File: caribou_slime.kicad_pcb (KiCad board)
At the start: 2 copper layers, 62.7 x 37.6 mm, 37 parts, among them J1 BATT JST, Q1 AO3145, U1 ESP32-C3_SUPERMINI, U2 BMI270, U3 FS312F-G, U4 FS8205A, U5 TP4056, U6 ME6211C33M5G

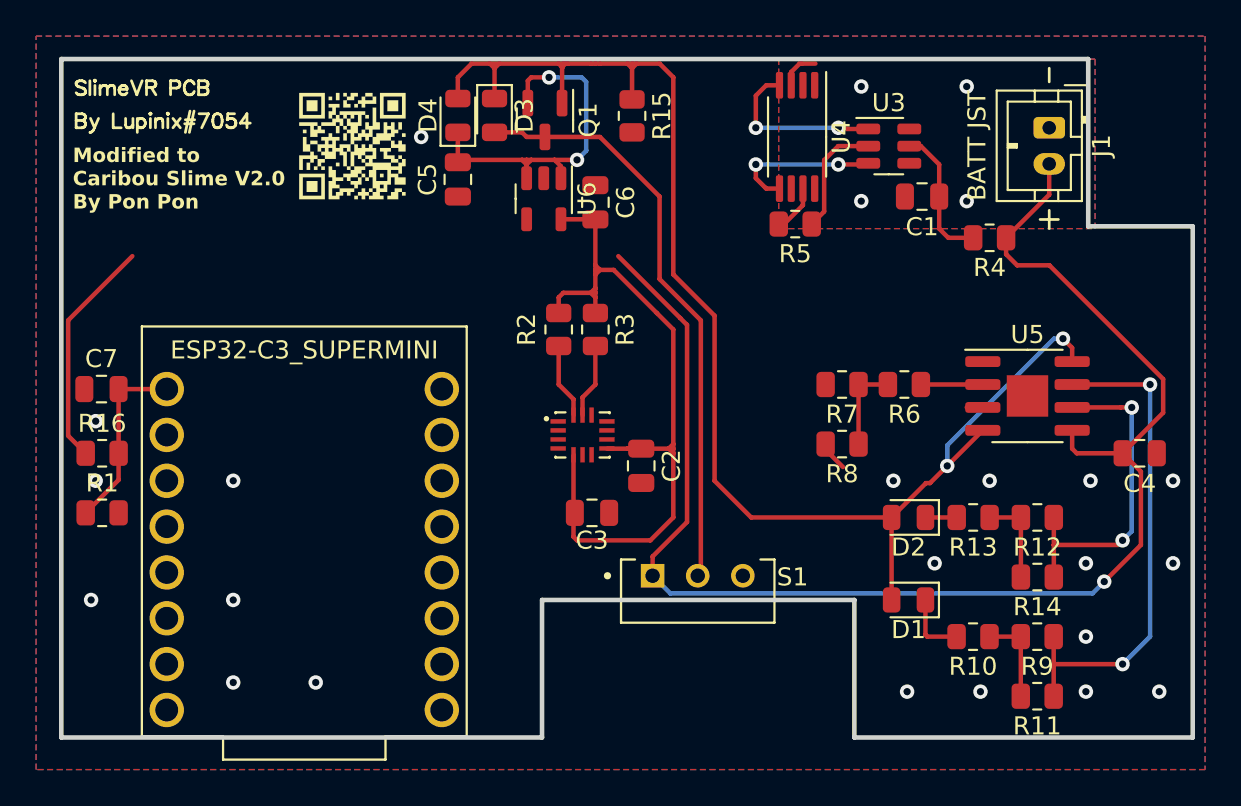
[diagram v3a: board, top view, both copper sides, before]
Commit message: chore(pcb): Improve SuperMini aesthetics
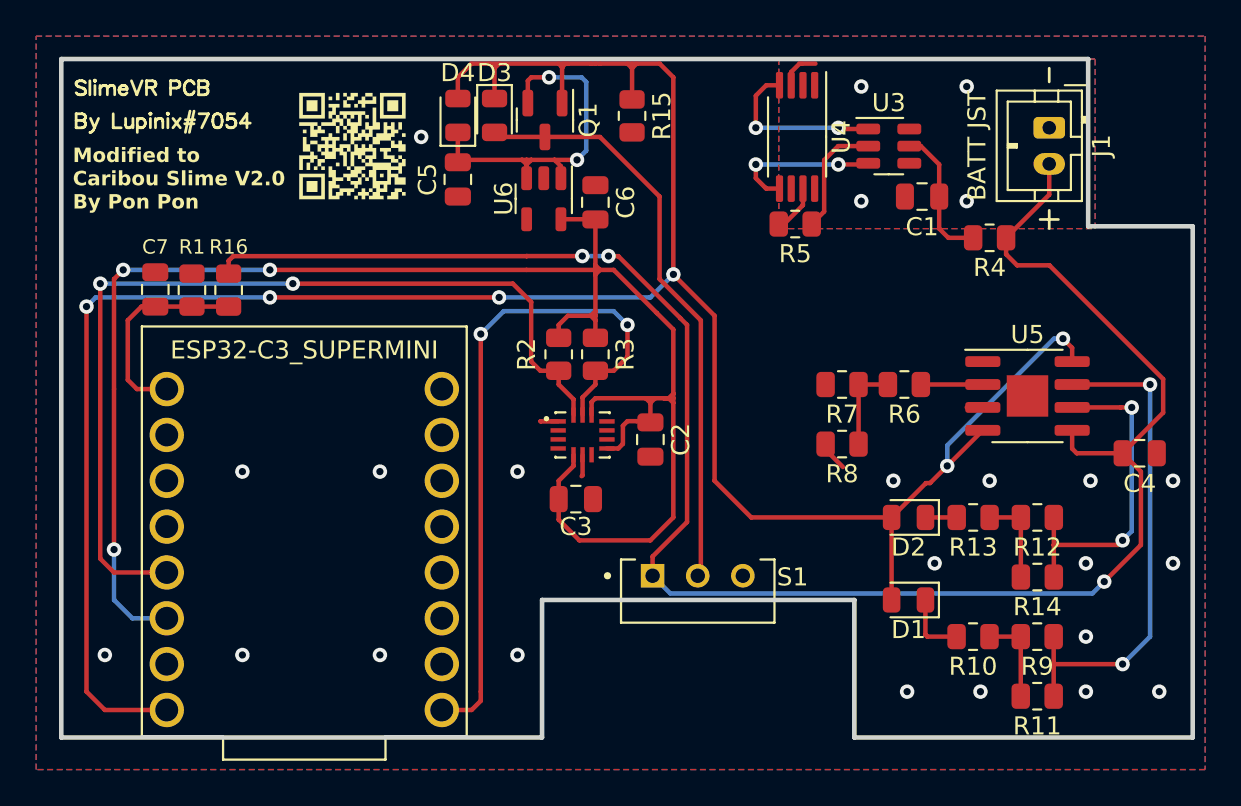
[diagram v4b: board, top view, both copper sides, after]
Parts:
- moved R1 13.3 mm to (32.8, 38.2), turned to 90 degrees
- moved R16 11.4 mm to (34.8, 38.2), turned to -90 degrees
- moved C7 6.28 mm to (30.7, 38.2), turned to -90 degrees
- moved C2 1.54 mm to (58.2, 46.5)
- moved R2 1.37 mm to (53.1, 41.8)
- moved R3 1.37 mm to (55.1, 41.8)
- moved C3 1.17 mm to (54.0, 49.8)
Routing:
- net +5V: track 78.8 -> 138.3 mm, vias 2 -> 6
- net +3V3: track 42.7 -> 99.8 mm, vias 0 -> 3
- net SDA: track 4.17 -> 51.1 mm, vias 0 -> 2
- net SCL: track 4.12 -> 37.8 mm, vias 0 -> 2
- net VBAT: track 93.5 -> 103.2 mm, vias 1 -> 3
- net GND: track 5.25 -> 7.45 mm
- net Net-(U1-GPIO0): track 10.3 -> 11.6 mm

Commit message: chore(pcb): Improve TP4056 aesthetics
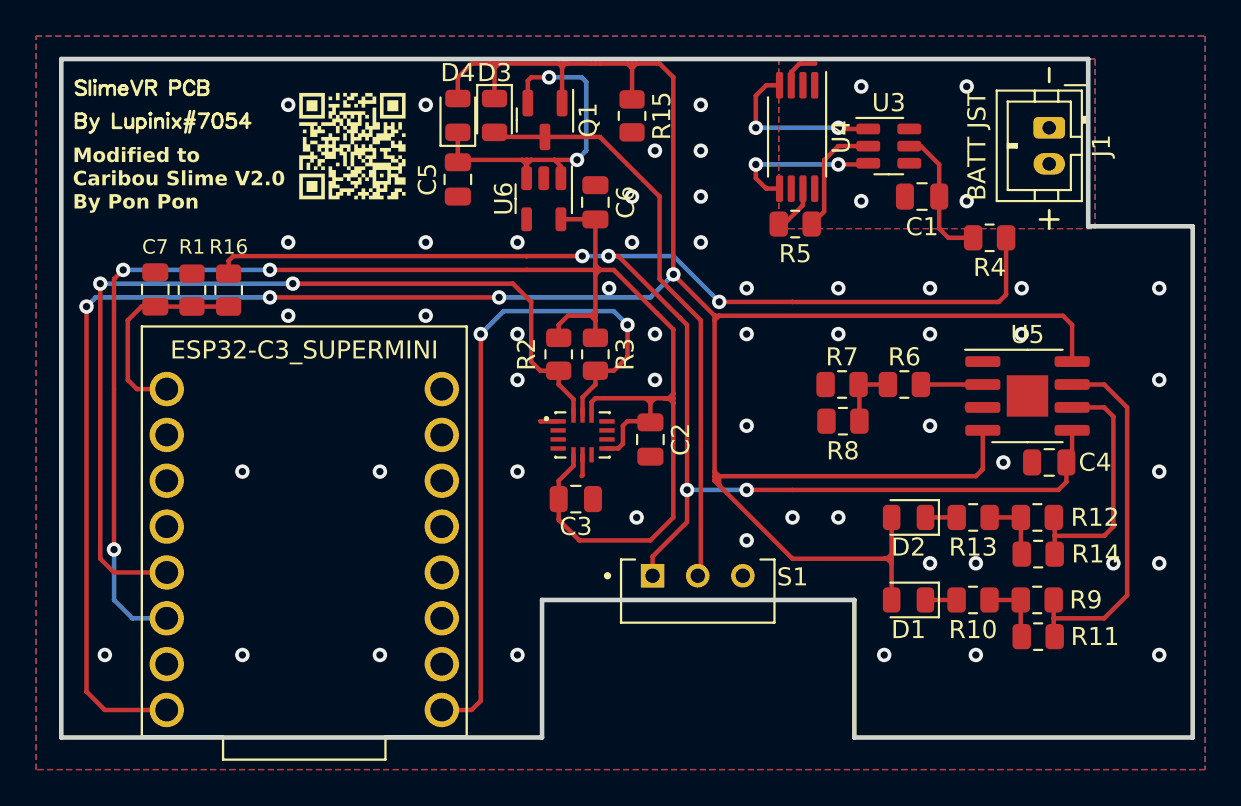
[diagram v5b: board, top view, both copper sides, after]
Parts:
- moved C4 5.04 mm to (80.3, 47.8), turned to 0 degrees
- moved R11 3.30 mm to (79.7, 57.4)
- moved R10 2.03 mm to (76.0, 55.4)
- moved R9 2.03 mm to (79.6, 55.4)
- moved R14 1.27 mm to (79.7, 52.8)
- moved R8 1.27 mm to (68.8, 45.5)
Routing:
- net +5V: track 138.3 -> 162.4 mm, vias 6 -> 4
- net VBAT: track 103.2 -> 93.0 mm, vias 3 -> 5
- net Net-(U5-CHRG): track 27.6 -> 20.6 mm, vias 2 -> 0
- net Net-(U5-STDBY): track 18.1 -> 14.1 mm, vias 2 -> 0
- net Net-(D1-K): track 3.70 -> 1.72 mm
- net GND: track 7.45 -> 5.78 mm, vias 20 -> 51
- net Net-(R6-Pad2): track 4.93 -> 3.68 mm
- net Net-(R12-Pad2): track 5.03 -> 3.78 mm
- net Net-(R10-Pad1): track 5.03 -> 3.79 mm

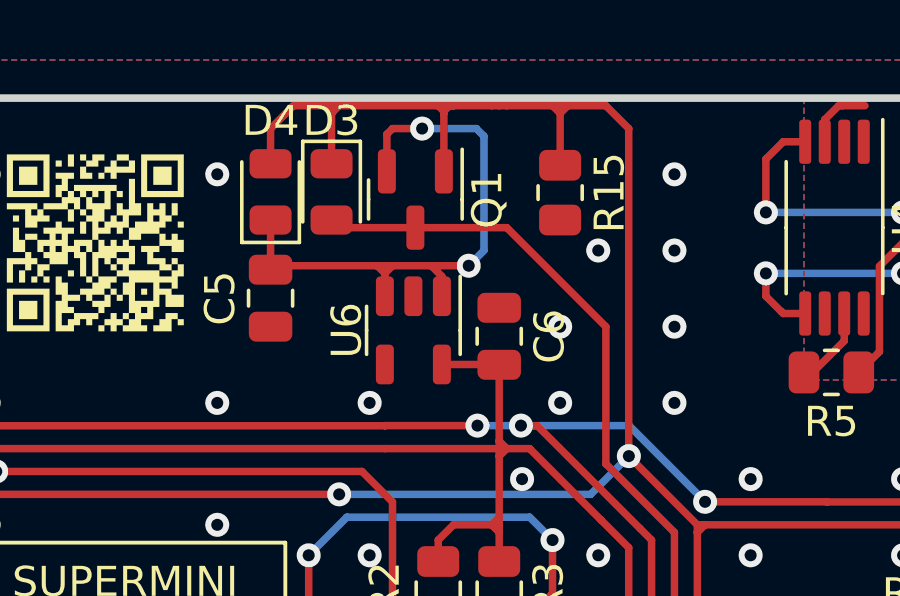
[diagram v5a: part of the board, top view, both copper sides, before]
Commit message: fix(pcb): Correct malformed trace in regulator circuit
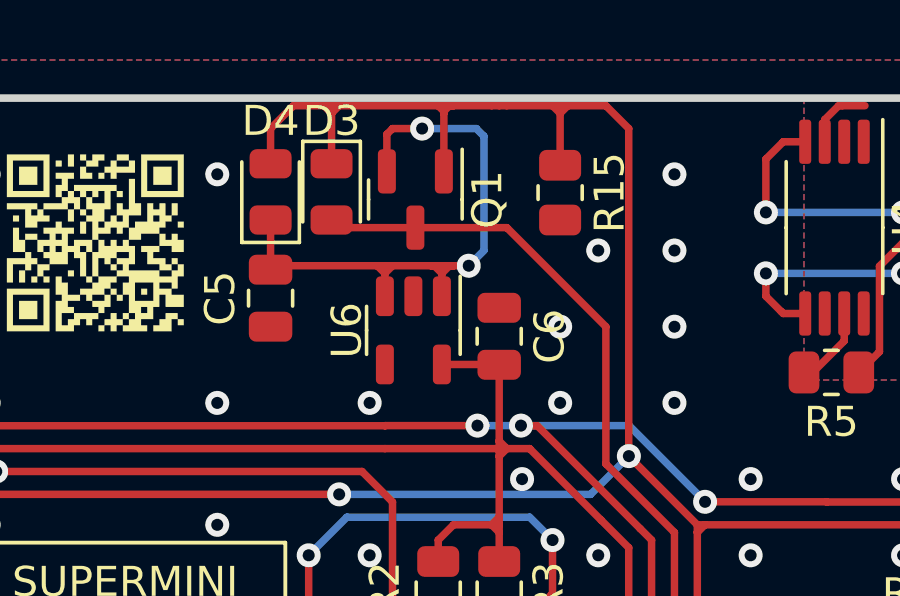
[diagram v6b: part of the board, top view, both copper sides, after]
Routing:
- net Net-(D4-K): track 20.4 -> 21.3 mm
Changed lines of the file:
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@@
   (segment (start 63.5 49.276) (end 60.198 49.276) (width 0.25) (layer "B.Cu") (net 16))
   (segment (start 61.976 38.852694) (end 61.980653 38.857347) (width 0.25) (layer "B.Cu") (net 16))
+  (segment (start 52.854499 30.988) (end 52.954 30.988) (width 0.25) (layer "F.Cu") (net 17))
   (segment (start 51.308 30.988) (end 51.562 30.988) (width 0.25) (layer "F.Cu") (net 17))
+  (segment (start 53.594 30.988) (end 53.462 30.988) (width 0.25) (layer "F.Cu") (net 17))
+  (segment (start 52.854499 30.988) (end 53.594 30.988) (width 0.25) (layer "F.Cu") (net 17))
+  (segment (start 53.594 30.988) (end 54.102 30.988) (width 0.25) (layer "F.Cu") (net 17))
   (segment (start 51.054 30.988) (end 51.308 30.988) (width 0.25) (layer "F.Cu") (net 17))
   (segment (start 51.374 27.843) (end 51.374 26.604) (width 0.25) (layer "F.Cu") (net 17))
   (segment (start 51.374 26.604) (end 51.562 26.416) (width 0.25) (layer "F.Cu") (net 17))
-  (segment (start 52.854499 30.988) (end 54.102 30.988) (width 0.25) (layer "F.Cu") (net 17))
   (segment (start 51.562 30.988) (end 52.854499 30.988) (width 0.25) (layer "F.Cu") (net 17))
-  (segment (start 53.208 32.004) (end 53.208 31.341501) (width 0.25) (layer "F.Cu") (net 17))
+  (segment (start 52.954 30.988) (end 53.208 31.242) (width 0.25) (layer "F.Cu") (net 17))
+  (segment (start 53.208 32.004) (end 53.208 31.242) (width 0.25) (layer "F.Cu") (net 17))
   (segment (start 51.308 31.242) (end 51.562 30.988) (width 0.25) (layer "F.Cu") (net 17))
   (segment (start 51.054 30.988) (end 51.308 31.242) (width 0.25) (layer "F.Cu") (net 17))
+  (segment (start 53.208 31.242) (end 53.208 31.11) (width 0.25) (layer "F.Cu") (net 17))
   (segment (start 51.562 26.416) (end 52.549 26.416) (width 0.25) (layer "F.Cu") (net 17))
   (segment (start 47.498 31.12) (end 47.874 31.12) (width 0.25) (layer "F.Cu") (net 17))
   (segment (start 47.874 31.12) (end 48.006 30.988) (width 0.25) (layer "F.Cu") (net 17))
-  (segment (start 52.854499 30.988) (end 53.208 31.341501) (width 0.25) (layer "F.Cu") (net 17))
   (segment (start 51.308 31.242) (end 51.308 32.004) (width 0.25) (layer "F.Cu") (net 17))
+  (segment (start 53.208 31.11) (end 53.086 30.988) (width 0.25) (layer "F.Cu") (net 17))
   (segment (start 51.308 30.988) (end 51.308 31.242) (width 0.25) (layer "F.Cu") (net 17))
   (segment (start 48.006 30.988) (end 51.054 30.988) (width 0.25) (layer "F.Cu") (net 17))
   (segment (start 47.498 29.464) (end 47.498 31.12) (width 0.25) (layer "F.Cu") (net 17))
+  (segment (start 53.462 30.988) (end 53.208 31.242) (width 0.25) (layer "F.Cu") (net 17))
   (via (at 54.102 30.988) (size 0.8) (drill 0.4) (layers "F.Cu" "B.Cu") (net 17))
   (via (at 52.549 26.416) (size 0.8) (drill 0.4) (layers "F.Cu" "B.Cu") (net 17))

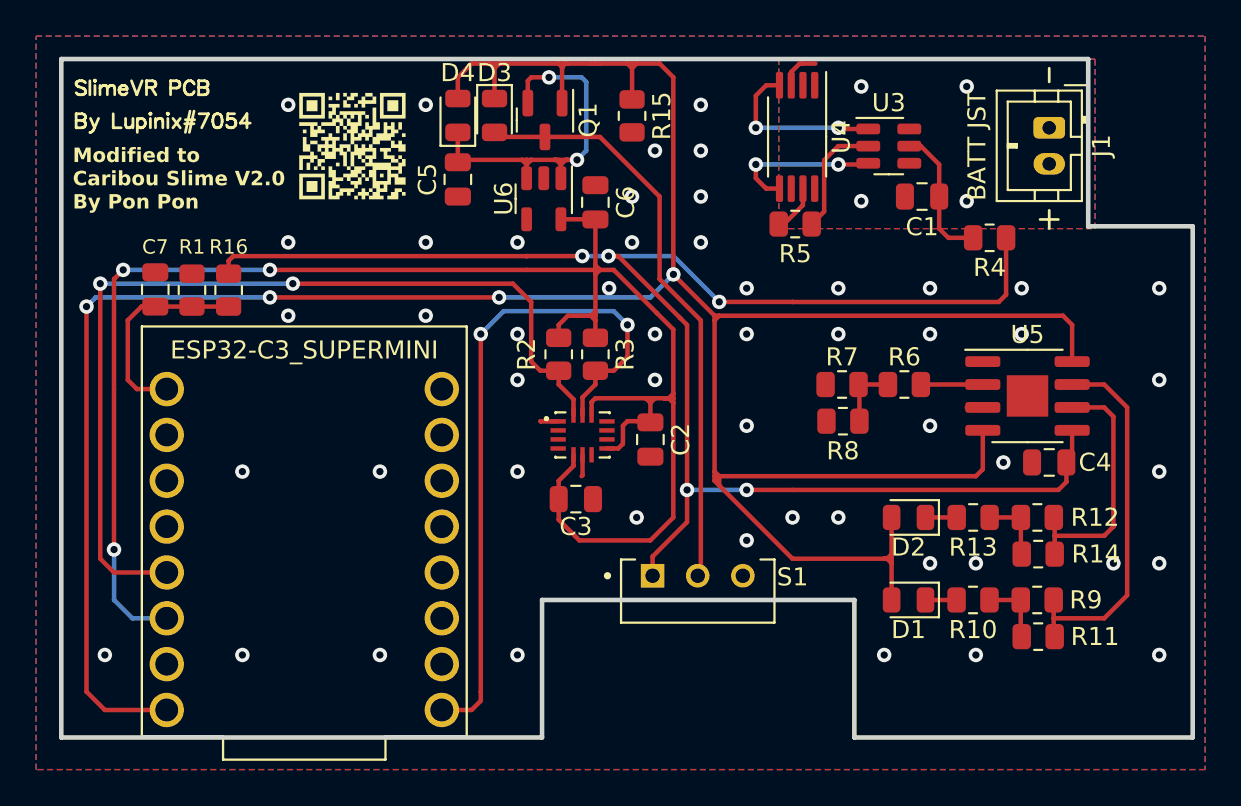
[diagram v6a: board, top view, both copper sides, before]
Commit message: chore(pcb): Improve TP4056 aesthetics
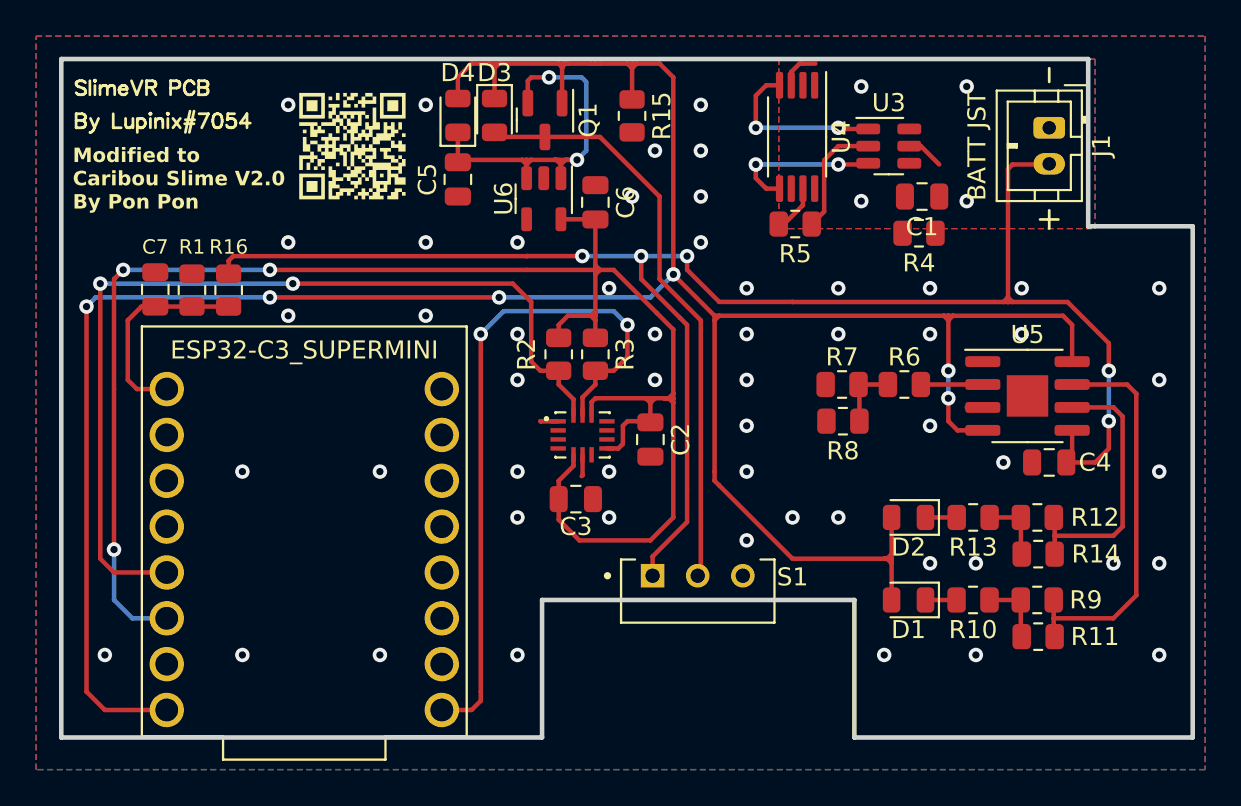
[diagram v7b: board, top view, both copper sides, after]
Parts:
- moved R4 3.92 mm to (73.0, 35.1)
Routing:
- net +5V: track 162.4 -> 152.7 mm, vias 4 -> 6
- net Net-(U3-Vcc): track 7.73 -> 2.08 mm
- net Net-(U5-CHRG): track 20.6 -> 22.1 mm
- net Net-(U5-STDBY): track 14.1 -> 15.1 mm
- net VBAT: track 93.0 -> 92.4 mm
- net GND: vias 51 -> 54
